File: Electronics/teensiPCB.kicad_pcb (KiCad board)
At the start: 2 copper layers, 45 x 84 mm, 15 parts, among them J1 screw terminal, J2 Conn_01x02, J5 UART1, J6 UART2, J7 I2C ext, SW1 SW_Push, U2 SAM-M10Q-00B

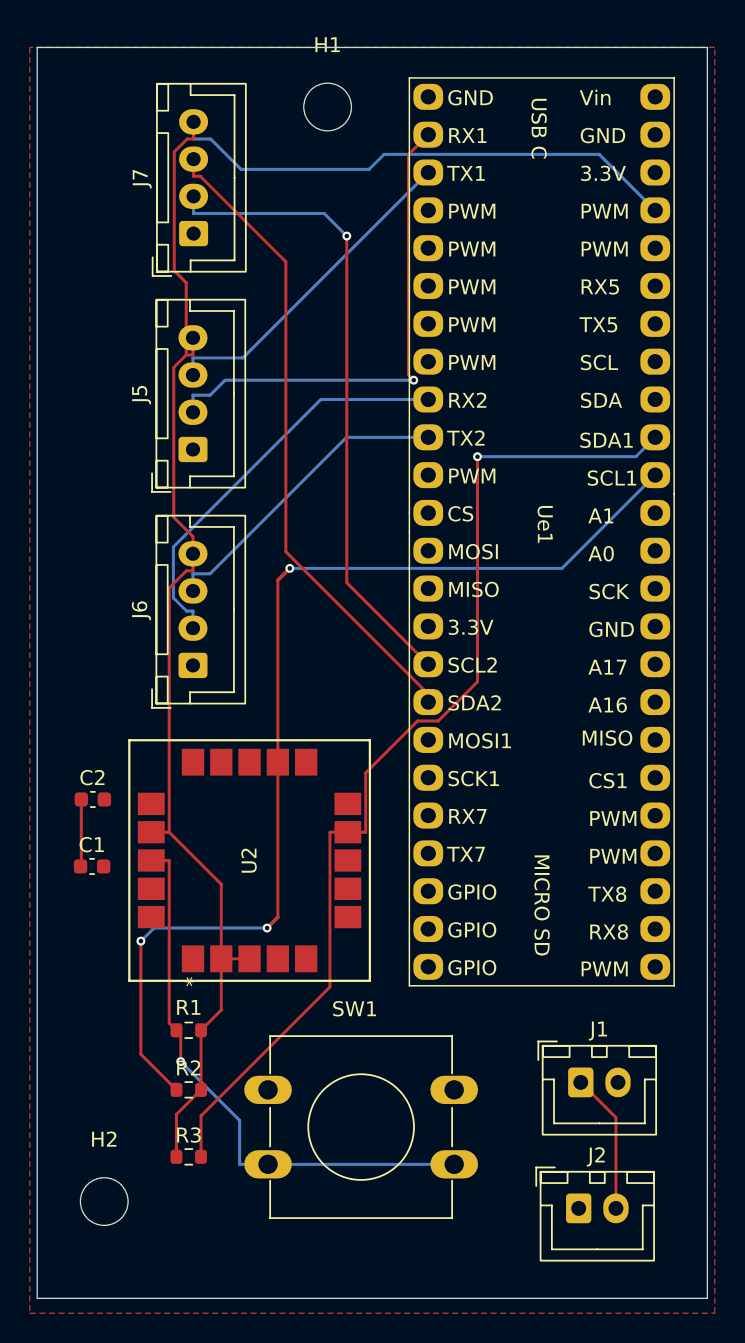
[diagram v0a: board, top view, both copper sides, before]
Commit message: footprint text and mounting holes
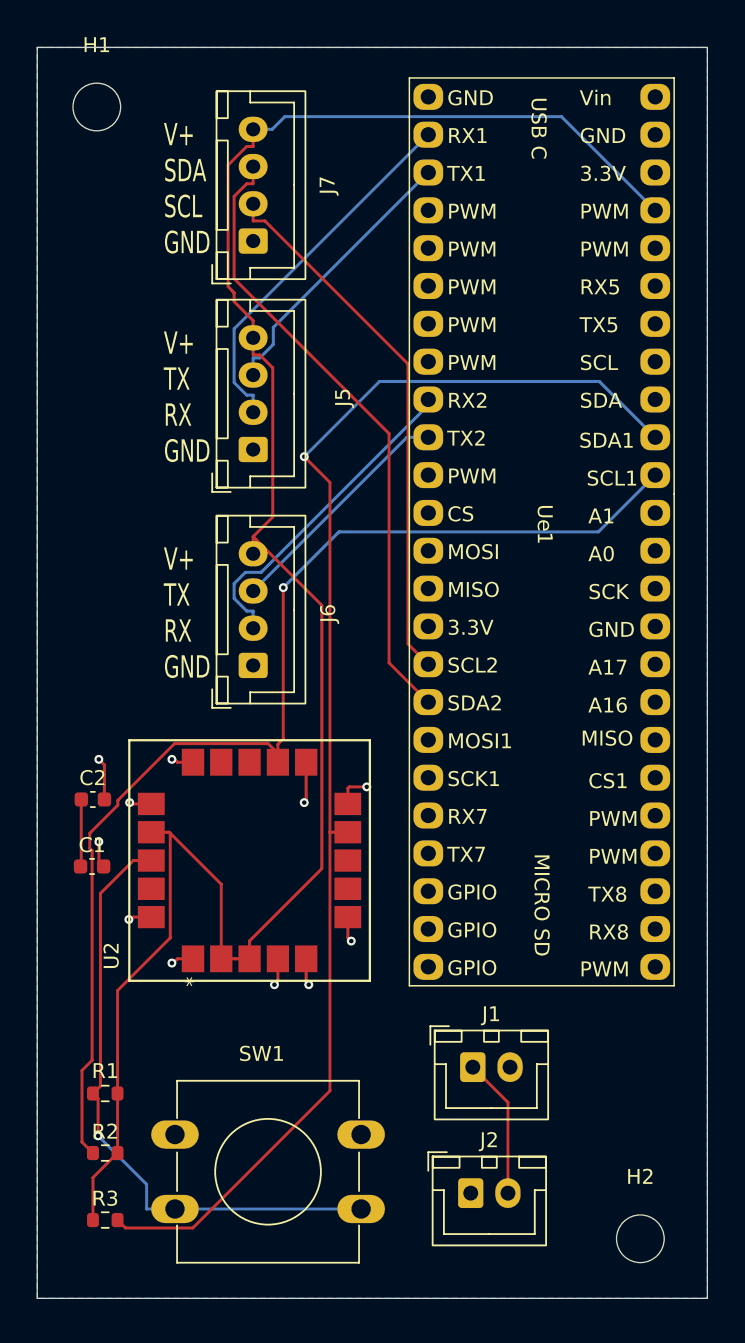
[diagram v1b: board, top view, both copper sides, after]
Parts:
- moved H2 36.1 mm to (213.0, 139.0)
- moved H1 15.5 mm to (176.5, 63.0)
- moved J1 7.32 mm to (201.8, 127.5)
- moved J2 7.32 mm to (201.6, 135.9)
- moved R1 7.03 mm to (177.1, 129.2)
- moved R2 7.03 mm to (177.1, 133.2)
- moved R3 7.03 mm to (177.1, 137.7)
- moved SW1 6.93 mm to (181.8, 132.0)
- moved J5 4.04 mm to (187.0, 86.0)
- moved J6 4.04 mm to (187.0, 100.5)
- moved J7 4.03 mm to (187.0, 72.0)
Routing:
- net GND: track 0.00 -> 21.6 mm, vias 0 -> 11
- net Net-(U2-SDA): track 69.4 -> 90.0 mm
- net +3V3: track 114.8 -> 135.2 mm
- net Net-(J5-Pin_2): track 33.6 -> 24.8 mm, vias 1 -> 0
- net Net-(J7-Pin_2): track 43.1 -> 36.3 mm, vias 1 -> 0
- net Net-(J6-Pin_2): track 27.5 -> 22.2 mm
- net Net-(J6-Pin_3): track 20.7 -> 16.0 mm
- net Net-(U2-RESET_N): track 38.0 -> 41.6 mm
- net Net-(J5-Pin_3): track 22.1 -> 18.7 mm
- net Net-(U2-SCL): track 80.4 -> 77.7 mm, vias 3 -> 1
- net Net-(J7-Pin_3): track 43.3 -> 42.1 mm
- added copper zone on B.Cu, net GND
- removed copper zone on F.Cu, net GND
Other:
- board text added: "V+ SDA SCL GND"
- board text added: "V+ TX RX GND"
